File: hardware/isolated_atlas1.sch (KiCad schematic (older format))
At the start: 15 parts, among them J301 CONN_01X02, P3 ATLAS_RTD_PROBE, U301 ADM3260, U302 ATLAS_RTD

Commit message: Upgrade to Kicad 5.
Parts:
- C301, C302, C303, C304, C305, C306: symbol C -> fk-atlas-rescue:C
- J301: symbol CONN_01X02 -> fk-atlas-rescue:CONN_01X02
- P3: symbol WATER_PROBE -> fk-atlas-rescue:WATER_PROBE
- R301, R302, R303, R304, R305: symbol R -> fk-atlas-rescue:R
- U301: symbol adm3260 -> fk-atlas-rescue:adm3260
- U302: symbol ATLAS_SENSOR -> conservify:ATLAS_SENSOR
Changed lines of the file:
@@
-EESchema Schematic File Version 2
-LIBS:conservify
+EESchema Schematic File Version 4
 LIBS:fk-atlas-cache
-EELAYER 25 0
+EELAYER 26 0
 EELAYER END
 $Descr A4 11693 8268
@@
 $EndDescr
 $Comp
-L adm3260 U301
+L fk-atlas-rescue:adm3260 U301
 U 1 1 594C2CF2
 P 4400 2900
@@
 $EndComp
 $Comp
-L C C303
+L fk-atlas-rescue:C C303
 U 1 1 594C2CF6
 P 5650 3800
@@
 $EndComp
 $Comp
-L C C304
+L fk-atlas-rescue:C C304
 U 1 1 594C2CF7
 P 5650 4100
@@
 $EndComp
 $Comp
-L C C305
+L fk-atlas-rescue:C C305
 U 1 1 5948D5A8
 P 5650 4400
@@
 $EndComp
 $Comp
-L C C306
+L fk-atlas-rescue:C C306
 U 1 1 594C2D02
 P 5650 4650
@@
 $EndComp
 $Comp
-L C C301
+L fk-atlas-rescue:C C301
 U 1 1 594C2D04
 P 2900 3800
@@
 $EndComp
 $Comp
-L C C302
+L fk-atlas-rescue:C C302
 U 1 1 594C2D09
 P 2900 4100
@@
 $EndComp
 $Comp
-L R R301
+L fk-atlas-rescue:R R301
 U 1 1 594C2D0C
 P 5650 3300
@@
 $EndComp
 $Comp
-L R R302
+L fk-atlas-rescue:R R302
 U 1 1 594C2D0F
 P 6250 2700
@@
 $EndComp
 $Comp
-L R R304
+L fk-atlas-rescue:R R304
 U 1 1 594C2D16
 P 6700 2700
@@
 $EndComp
 $Comp
-L R R303
+L fk-atlas-rescue:R R303
 U 1 1 594C2D1A
 P 6300 3250
@@
 $EndComp
 $Comp
-L R R305
+L fk-atlas-rescue:R R305
 U 1 1 5948E4EE
 P 6800 3250
@@
 $EndComp
 $Comp
-L VCC #PWR059
+L fk-atlas-rescue:VCC #PWR059
 U 1 1 594C2D23
 P 2450 3750
@@
 $EndComp
 $Comp
-L VCC #PWR060
+L fk-atlas-rescue:VCC #PWR060
 U 1 1 594C2D29
 P 2450 2350
@@
 $EndComp
 $Comp
-L ATLAS_SENSOR U302
+L conservify:ATLAS_SENSOR U302
 U 1 1 594C2D36
 P 8550 2900
@@
 $EndComp
 $Comp
-L CONN_01X02 J301
+L fk-atlas-rescue:CONN_01X02 J301
 U 1 1 59A1BC7C
 P 10100 2950
@@
 $EndComp
 $Comp
-L WATER_PROBE P3
+L fk-atlas-rescue:WATER_PROBE P3
 U 1 1 59D29DF5
 P 8800 3550

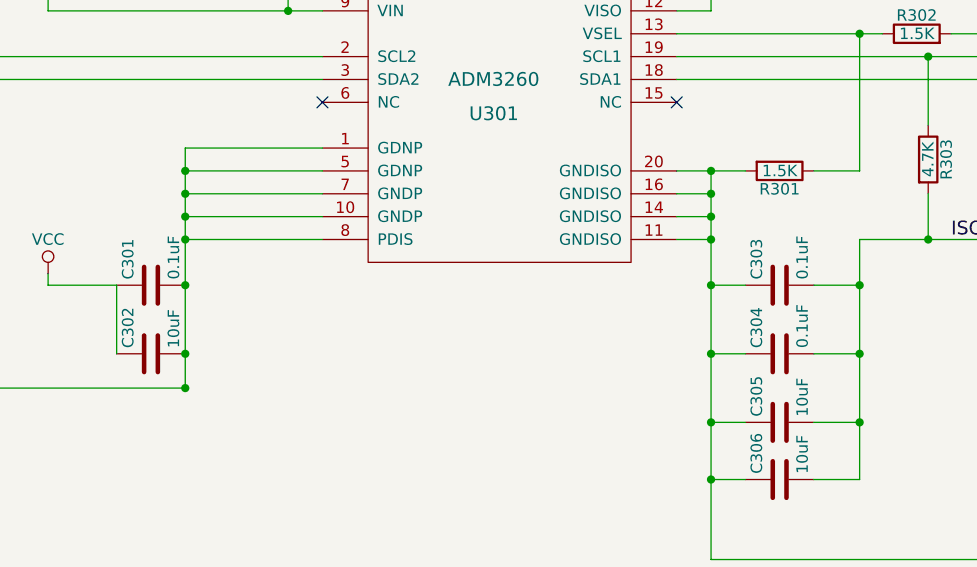
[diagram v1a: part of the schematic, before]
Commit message: Consistent part values across our schematics.
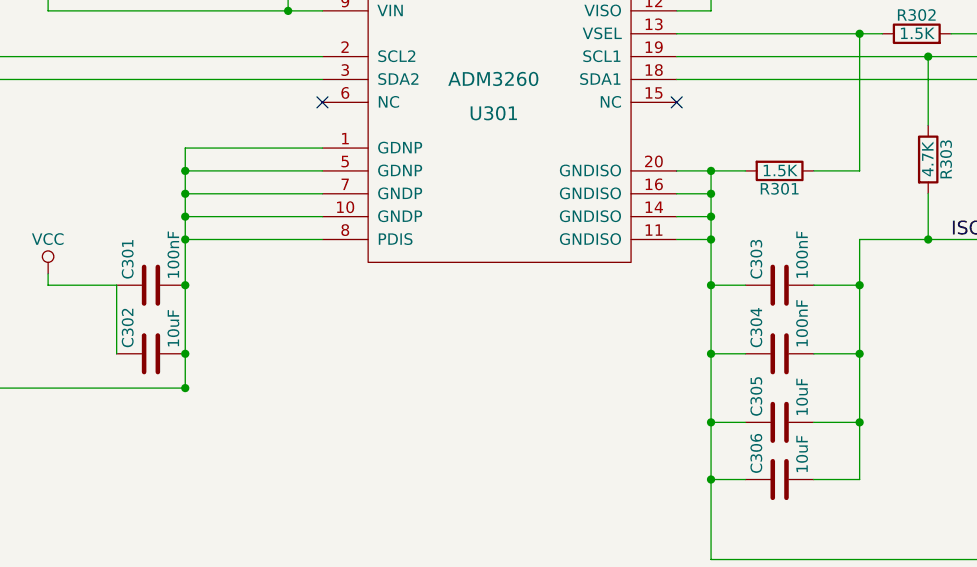
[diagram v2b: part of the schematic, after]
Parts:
- C301, C303, C304: value 0.1uF -> 100nF

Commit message: Part updates.
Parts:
- C301, C303, C304: Critical (none) -> (none); MFN (none) -> Murata Electronics; MFP (none) -> GRM188R71H104KA93D; Notes (none) -> (none); Package (none) -> (none); Source (none) -> ANY; Subsystem (none) -> (none); Supplier1 (none) -> mouser
- C302, C305, C306: Critical (none) -> (none); MFN (none) -> Taiyo Yuden; MFP (none) -> LMK107BBJ106KALT; Notes (none) -> (none); Package (none) -> (none); Source (none) -> ANY; Subsystem (none) -> (none); Supplier1 (none) -> mouser; spn1 81-GRM188R60J106ME47 -> 963-LMK107BBJ106KALT
- J301: Critical (none) -> (none); MFN (none) -> Amphenol RF; MFP (none) -> 031-5431; Notes (none) -> (none); Package (none) -> (none); Source (none) -> ANY; Subsystem (none) -> (none); Supplier1 (none) -> mouser
- P3: Critical (none) -> (none); MFN (none) -> (none); MFP (none) -> (none); Notes (none) -> (none); Package (none) -> (none); SPN1 (none) -> (none); Source (none) -> ANY; Subsystem (none) -> (none); Supplier1 (none) -> (none)
- R301, R302, R304: Critical (none) -> (none); MFN (none) -> (none); MFP (none) -> (none); Notes (none) -> (none); Package (none) -> (none); Source (none) -> ANY; Subsystem (none) -> (none); Supplier1 (none) -> (none)
- R303, R305: Critical (none) -> (none); MFN (none) -> Yageo; MFP (none) -> AF0603JR-074K7L; Notes (none) -> (none); Package (none) -> (none); Source (none) -> ANY; Subsystem (none) -> (none); Supplier1 (none) -> mouser
- U301: Critical (none) -> (none); MFN (none) -> Analog Devices / Linear Technology; MFP (none) -> ADM3260ARSZ; Notes (none) -> (none); Package (none) -> (none); Source (none) -> ANY; Subsystem (none) -> (none); Supplier1 (none) -> mouser
- U302: Critical (none) -> (none); MFN (none) -> (none); MFP (none) -> (none); Notes (none) -> (none); Package (none) -> (none); SPN1 (none) -> (none); Source (none) -> ANY; Subsystem (none) -> (none); Supplier1 (none) -> atlas

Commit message: Fix DRC in schematic mode.
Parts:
- C301, C302, C303, C304, C305, C306: symbol fk-atlas-rescue:C -> conservify:CAPACITOR_CERAMIC
- J301: symbol fk-atlas-rescue:CONN_01X02 -> conservify:CONN_01x02
- P3: symbol fk-atlas-rescue:WATER_PROBE -> conservify:ATLAS_WATER_PROBE
- R301, R302, R303, R304, R305: symbol fk-atlas-rescue:R -> conservify:R
- U301: symbol fk-atlas-rescue:adm3260 -> conservify:ADM3260
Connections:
- wire segments 52 -> 78
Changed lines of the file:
@@
 $EndDescr
 $Comp
-L fk-atlas-rescue:adm3260 U301
+L conservify:ADM3260 U301
 U 1 1 594C2CF2
 P 4400 2900
@@
 $EndComp
 $Comp
-L fk-atlas-rescue:C C303
+L conservify:CAPACITOR_CERAMIC C303
 U 1 1 594C2CF6
 P 5650 3800
@@
 $EndComp
 $Comp
-L fk-atlas-rescue:C C304
+L conservify:CAPACITOR_CERAMIC C304
 U 1 1 594C2CF7
 P 5650 4100
@@
 $EndComp
 $Comp
-L fk-atlas-rescue:C C305
+L conservify:CAPACITOR_CERAMIC C305
 U 1 1 5948D5A8
 P 5650 4400
@@
 $EndComp
 $Comp
-L fk-atlas-rescue:C C306
+L conservify:CAPACITOR_CERAMIC C306
 U 1 1 594C2D02
 P 5650 4650
@@
 $EndComp
 $Comp
-L fk-atlas-rescue:C C301
+L conservify:CAPACITOR_CERAMIC C301
 U 1 1 594C2D04
 P 2900 3800
@@
 $EndComp
 $Comp
-L fk-atlas-rescue:C C302
+L conservify:CAPACITOR_CERAMIC C302
 U 1 1 594C2D09
 P 2900 4100
@@
 $EndComp
 $Comp
-L fk-atlas-rescue:R R301
+L conservify:R R301
 U 1 1 594C2D0C
 P 5650 3300
@@
 $EndComp
 $Comp
-L fk-atlas-rescue:R R302
+L conservify:R R302
 U 1 1 594C2D0F
 P 6250 2700
@@
 $EndComp
 $Comp
-L fk-atlas-rescue:R R304
+L conservify:R R304
 U 1 1 594C2D16
 P 6700 2700
@@
 $EndComp
 $Comp
-L fk-atlas-rescue:R R303
+L conservify:R R303
 U 1 1 594C2D1A
 P 6300 3250
@@
 $EndComp
 $Comp
-L fk-atlas-rescue:R R305
+L conservify:R R305
 U 1 1 5948E4EE
 P 6800 3250
@@
 $EndComp
 $Comp
-L fk-atlas-rescue:VCC #PWR059
+L conservify:VCC #PWR059
 U 1 1 594C2D23
 P 2450 3750
@@
 $EndComp
 $Comp
-L fk-atlas-rescue:VCC #PWR060
+L conservify:VCC #PWR060
 U 1 1 594C2D29
 P 2450 2350
@@
 $EndComp
 $Comp
-L fk-atlas-rescue:CONN_01X02 J301
+L conservify:CONN_01x02 J301
 U 1 1 59A1BC7C
-P 10100 2950
-F 0 "J301" H 10100 3100 50  0000 C CNN
-F 1 "CONN_01X02" V 10200 2950 50  0000 C CNN
-F 2 "conservify:BNC" H 10100 2950 50  0001 C CNN
-F 3 "" H 10100 2950 50  0001 C CNN
-F 4 " " H 10100 3200 50  0001 C CNN "Critical"
-F 5 "Amphenol RF" H 10100 3200 50  0001 C CNN "MFN"
-F 6 "031-5431" H 10100 3200 50  0001 C CNN "MFP"
-F 7 " " H 10100 3200 50  0001 C CNN "Notes"
-F 8 " " H 10100 3200 50  0001 C CNN "Package"
-F 9 "ANY" H 10100 3200 50  0001 C CNN "Source"
-F 10 " " H 10100 3200 50  0001 C CNN "Subsystem"
-F 11 "mouser" H 10100 3200 50  0001 C CNN "Supplier1"
-F 12 "0" H 10100 3200 50  0001 C CNN "price"
-F 13 "523-31-5431" H 250 0   50  0001 C CNN "spn1"
-	1    10100 2950
-	1    0    0    -1
-$EndComp
-$Comp
-L fk-atlas-rescue:WATER_PROBE P3
+P 10100 2900
+F 0 "J301" H 10100 3050 50  0000 C CNN
+F 1 "CONN_01X02" V 10200 2900 50  0000 C CNN
+F 2 "conservify:BNC" H 10100 2900 50  0001 C CNN
+F 3 "" H 10100 2900 50  0001 C CNN
+F 4 " " H 10100 3150 50  0001 C CNN "Critical"
+F 5 "Amphenol RF" H 10100 3150 50  0001 C CNN "MFN"
+F 6 "031-5431" H 10100 3150 50  0001 C CNN "MFP"
+F 7 " " H 10100 3150 50  0001 C CNN "Notes"
+F 8 " " H 10100 3150 50  0001 C CNN "Package"
+F 9 "ANY" H 10100 3150 50  0001 C CNN "Source"
+F 10 " " H 10100 3150 50  0001 C CNN "Subsystem"
+F 11 "mouser" H 10100 3150 50  0001 C CNN "Supplier1"
+F 12 "0" H 10100 3150 50  0001 C CNN "price"
+F 13 "523-31-5431" H 250 -50 50  0001 C CNN "spn1"
+	1    10100 2900
+	1    0    0    -1
+$EndComp
+$Comp
+L conservify:ATLAS_WATER_PROBE P3
 U 1 1 59D29DF5
 P 8800 3550
@@
 F 12 " " H 8800 3650 50  0001 C CNN "Supplier1"
 	1    8800 3550
+	1    0    0    -1
+$EndComp
+$Comp
+L conservify:PWR_FLAG #FLG0105
+U 1 1 5BCBBD88
+P 7400 4850
+F 0 "#FLG0105" H 7400 4925 50  0001 C CNN
+F 1 "PWR_FLAG" H 7400 5000 50  0000 C CNN
+F 2 "" H 7400 4850 50  0001 C CNN
+F 3 "~" H 7400 4850 50  0001 C CNN
+	1    7400 4850
 	1    0    0    -1
 $EndComp
@@
 RTD_PGND
 Wire Wire Line
-	5200 3300 5500 3300
-Wire Wire Line
-	5350 3300 5350 5000
+	5200 3300 5350 3300
+Wire Wire Line
+	5350 3300 5350 3400
 Wire Wire Line
 	5350 3600 5200 3600
@@
 	5800 3800 6000 3800
 Wire Wire Line
-	6000 3600 6000 4650
+	6000 3600 6000 3800
 Wire Wire Line
 	6000 4650 5800 4650
@@
 	5800 4100 6000 4100
 Wire Wire Line
-	5200 2800 7800 2800
-Wire Wire Line
-	5200 2900 7800 2900
-Wire Wire Line
-	5200 2700 6100 2700
+	5200 2800 6300 2800
+Wire Wire Line
+	5200 2900 6800 2900
+Wire Wire Line
+	5200 2700 6000 2700
 Wire Wire Line
 	6000 2700 6000 3300
@@
 	5350 2600 5350 2500
 Wire Wire Line
-	5200 2500 7400 2500
+	5200 2500 5350 2500
 Wire Wire Line
 	6900 2500 6900 2700
@@
 	6300 3400 6300 3600
 Wire Wire Line
-	6000 3600 6800 3600
+	6000 3600 6300 3600
 Wire Wire Line
 	6800 3600 6800 3400
 Wire Wire Line
-	2450 2600 3650 2600
-Wire Wire Line
-	2450 2350 2450 2600
+	2450 2600 3500 2600
+Wire Wire Line
+	2450 2350 2450 2450
 Wire Wire Line
 	3650 2500 3500 2500
@@
 	3650 3200 3050 3200
 Wire Wire Line
-	3050 3200 3050 4250
+	3050 3200 3050 3300
 Wire Wire Line
 	3050 4250 1750 4250
@@
 Wire Wire Line
 	9450 3000 9900 3000
+Wire Wire Line
+	7400 4850 7400 5000
+Wire Wire Line
+	5350 3500 5350 3600
+Wire Wire Line
+	5350 3400 5350 3500
+Wire Wire Line
+	5350 3600 5350 3800
+Wire Wire Line
+	5350 4400 5350 4650
+Wire Wire Line
+	5350 4100 5350 4400
+Wire Wire Line
+	5350 3800 5350 4100
+Wire Wire Line
+	6000 4400 6000 4650
+Wire Wire Line
+	6000 4100 6000 4400
+Wire Wire Line
+	5350 3300 5500 3300
+Wire Wire Line
+	5350 2500 6900 2500
+Wire Wire Line
+	6000 2700 6100 2700
+Wire Wire Line
+	6300 2800 7800 2800
+Wire Wire Line
+	6800 2900 7800 2900
+Wire Wire Line
+	3500 2600 3650 2600
+Wire Wire Line
+	3050 3800 3050 4100
+Wire Wire Line
+	3050 4100 3050 4250
+Wire Wire Line
+	3050 3600 3050 3800
+Wire Wire Line
+	3050 3500 3050 3600
+Wire Wire Line
+	3050 3400 3050 3500
+Wire Wire Line
+	3050 3300 3050 3400
+Wire Wire Line
+	2450 2450 2450 2600
+Wire Wire Line
+	5350 4650 5350 5000
+Wire Wire Line
+	6300 3600 6800 3600
+Wire Wire Line
+	6000 3800 6000 4100
+Wire Wire Line
+	6900 2500 7400 2500
 Connection ~ 5350 3500
 Connection ~ 5350 3400
@@
 Connection ~ 6300 3600
 Connection ~ 6000 3800
-Connection ~ 3050 4250
 Connection ~ 6900 2500
 NoConn ~ 3650 3000

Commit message: New footprint for the Atlas RTD OEM board.
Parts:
- U302: footprint conservify:ATLAS_SENSOR_BOARD_COMBO -> conservify:ATLAS_SENSOR_BOARD_RTD_COMBO

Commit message: Drop prototype Atlas modules - focus on getting OEM boards working.
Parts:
- U302: footprint conservify:ATLAS_SENSOR_BOARD_RTD_COMBO -> conservify:ATLAS_SENSOR_BOARD_RTD_OEM
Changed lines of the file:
@@
 F 0 "U302" H 8100 2550 60  0000 C CNN
 F 1 "ATLAS_RTD" H 8600 2850 60  0000 C CNN
-F 2 "conservify:ATLAS_SENSOR_BOARD_RTD_COMBO" H 8550 2900 60  0001 C CNN
+F 2 "conservify:ATLAS_SENSOR_BOARD_RTD_OEM" H 8550 2900 60  0001 C CNN
 F 3 "" H 8550 2900 60  0001 C CNN
 F 4 " " H 8100 2650 50  0001 C CNN "Critical"
